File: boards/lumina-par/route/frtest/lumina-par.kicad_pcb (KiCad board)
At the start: 4 copper layers, 100 x 80 mm, 159 parts, among them J3 DS1023-2*7SF11 2x7 socket 2.5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, J4 DS1023-2*12SF11 2x12 socket, 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, J5 S10B-PH-SM4-TB JST PH 10-way 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, Q101 NCE01P13K -100V P-MOSFET TO-2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, Q102 BSS123 100V N-MOSFET SOT-23, Q301 SSM3K2615R 60V 2A N-FET, Q321 SSM3K2615R 60V 2A N-FET, Q341 SSM3K2615R 60V 2A N-FET, Q361 SSM3K2615R 60V 2A N-FET, U201 SN74LVC1G08DBVR single 2-inpu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, U202 SN74LVC00ADR quad 2-input NAN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, U203 M24C32-WMN6TP 32 kbit I2C EEP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, U204 SN74LVC14ADR hex Schmitt-trig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, U301 TPS92515HVDGQR, U321 TPS92515HVDGQR, U341 TPS92515HVDGQR, U361 TPS92515HVDGQR, U401 LM339LVPWR quad open-drain co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

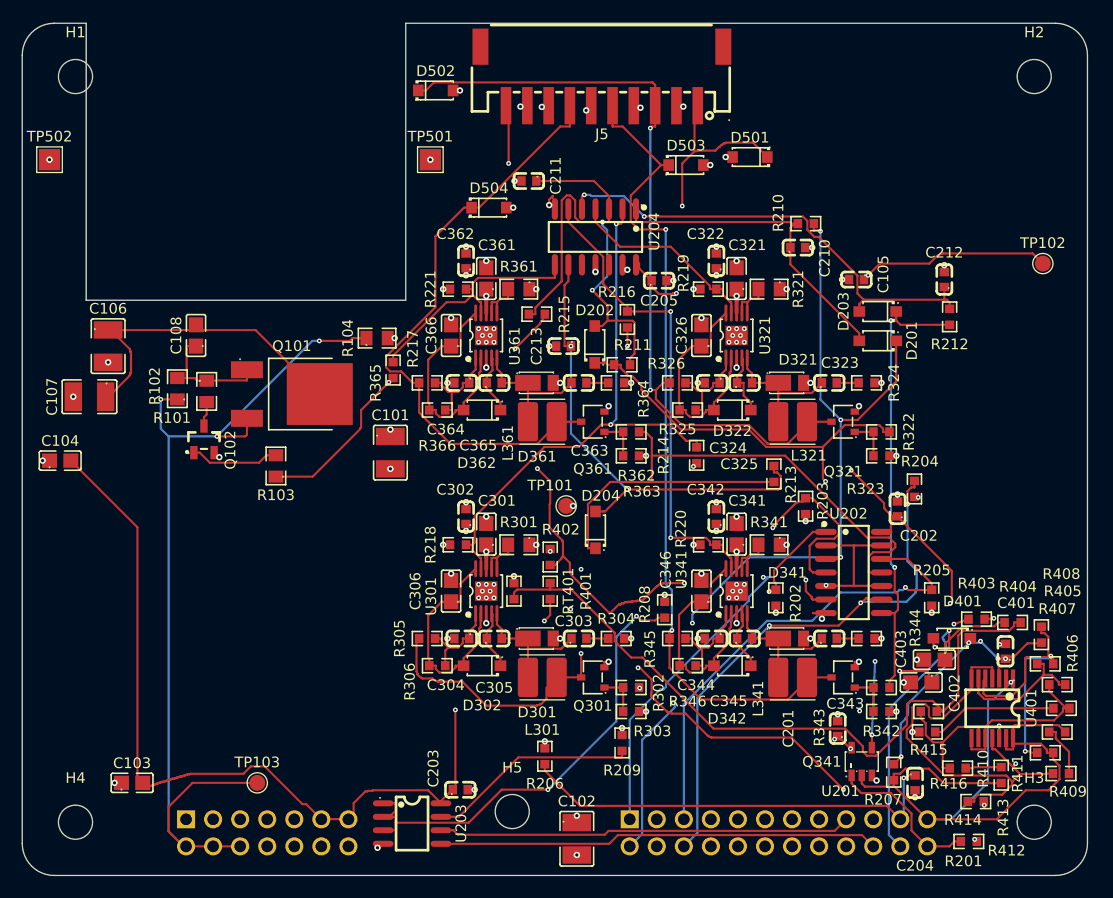
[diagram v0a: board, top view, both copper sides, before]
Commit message: ai-ee lumina-par: drc_routed pass - 100% routed, 0 violations
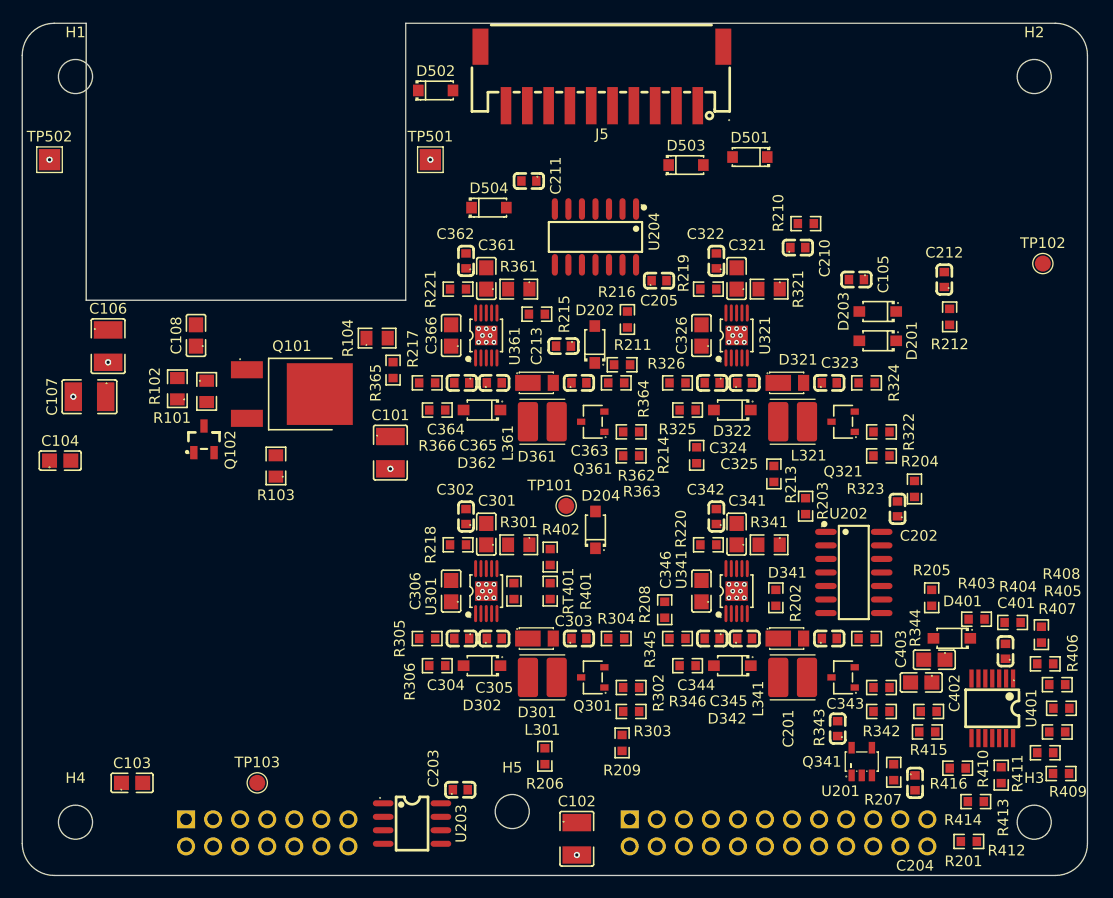
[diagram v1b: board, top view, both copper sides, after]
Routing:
- net +3V3: track 270.9 -> 0.00 mm, vias 14 -> 0
- net /EN_OK: track 116.6 -> 0.00 mm, vias 7 -> 0
- net /NTC_LED: track 114.9 -> 0.00 mm, vias 6 -> 0
- net +48V_SW: track 90.3 -> 0.00 mm, vias 3 -> 0
- net /LED0_A: track 86.9 -> 0.00 mm, vias 3 -> 0
- net /LED2_A: track 77.8 -> 0.00 mm, vias 2 -> 0
- net /LED1_A: track 73.8 -> 0.00 mm, vias 2 -> 0
- net /SHUNT0: track 72.0 -> 0.00 mm, vias 5 -> 0
- net /FAULT: track 71.1 -> 0.00 mm, vias 1 -> 0
- net /thermal/NTC_BRD: track 67.4 -> 0.00 mm
- net GND: track 64.8 -> 0.00 mm, vias 119 -> 38
- net /SHUNT3: track 60.9 -> 0.00 mm
- net /ADC0: track 60.4 -> 0.00 mm, vias 5 -> 0
- net /LED3_A: track 57.0 -> 0.00 mm
- net /thermal/CMP_LED: track 56.9 -> 0.00 mm, vias 2 -> 0
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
